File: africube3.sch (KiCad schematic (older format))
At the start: 36 parts, among them IC1 ADC-20-4, J1 SMA Edge FM, J2 Conn_01x04, J3 RPi_GPIO, J4 Conn_01x02, U1 TQP7M9105, U2 SXBP-150+, U3 BA178M05FP-E2, U4 MCP3421A0T-E/CH

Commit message: removing power detector
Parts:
- removed C8: 100pF, Capacitors_SMD:C_0805_HandSoldering, symbol C_Small
- removed C?: 1nF, Capacitors_SMD:C_0805_HandSoldering, symbol C_Small
- removed D2: SMS3922-079LF, symbol D_Schottky
- removed IC1: ADC-20-4, ADC-20-4+, symbol ADC-20-4
- removed R3: 50, Resistors_SMD:R_0805_HandSoldering, symbol R
- removed R6, R7, R8, R9: 220K, Resistors_SMD:R_0805_HandSoldering, symbol R
- removed U4: MCP3421A0T-E/CH, symbol MCP3421A0T-E/CH
- U3: footprint TO_SOT_Packages_SMD:TO-252-3_TabPin2 -> TO_SOT_Packages_SMD:TO-252-3_TabPin4
- renumbered C11 to C10, C9 to C8, C10 to C9, R4 to R3, R5 to R4
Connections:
- net at J1.1 (In): now also U2.8 (RF_OUT)
- net SCL: no longer names the net of J3.5 (GPIO03_SCL1_I2C)
- net SDA: no longer names the net of J3.3 (GPIO02_SDA1_I2C)
- no-connect marks 25 -> 27
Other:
- moved on the sheet: J1

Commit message: removed power detection
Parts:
- U2: footprint RF_Mini-Circuits:Mini-Circuits_HF1139_LandPatternPL-230 -> mini_filter:Mini-Circuits_HF1139_LandPatternPL-230
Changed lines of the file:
@@
 LIBS:ADC-15-4+
 LIBS:AD8317
+LIBS:africube3-cache
 EELAYER 25 0
 EELAYER END
@@
 F 0 "U2" H 7200 1800 60  0000 C CNN
 F 1 "SXBP-150+" H 7200 2300 60  0000 C CNN
-F 2 "RF_Mini-Circuits:Mini-Circuits_HF1139_LandPatternPL-230" H 7200 1900 60  0001 C CNN
+F 2 "mini_filter:Mini-Circuits_HF1139_LandPatternPL-230" H 7200 1900 60  0001 C CNN
 F 3 "" H 7200 1900 60  0001 C CNN
 	1    7200 2050

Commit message: layout done need to do groundplanes
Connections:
- net GND: now also J2.4 (Pin_4), U3.2 (GND)
- now unconnected: J3.1 (3.3V), J3.17 (3.3V)
- no-connect marks 27 -> 29
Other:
- moved on the sheet: C9
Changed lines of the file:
@@
 L GND #PWR016
 U 1 1 5D290BB7
-P 5650 3350
-F 0 "#PWR016" H 5650 3100 50  0001 C CNN
-F 1 "GND" H 5650 3200 50  0000 C CNN
-F 2 "" H 5650 3350 50  0001 C CNN
-F 3 "" H 5650 3350 50  0001 C CNN
-	1    5650 3350
+P 5550 3350
+F 0 "#PWR016" H 5550 3100 50  0001 C CNN
+F 1 "GND" H 5550 3200 50  0000 C CNN
+F 2 "" H 5550 3350 50  0001 C CNN
+F 3 "" H 5550 3350 50  0001 C CNN
+	1    5550 3350
 	1    0    0    -1
 $EndComp
@@
 L CP_Small C9
 U 1 1 5D290DB1
-P 5650 3150
-F 0 "C9" H 5500 3050 50  0000 L CNN
-F 1 "4.7uF 16V" H 5400 3450 50  0000 L CNN
-F 2 "Capacitors_SMD:C_0805_HandSoldering" H 5650 3150 50  0001 C CNN
-F 3 "" H 5650 3150 50  0001 C CNN
-	1    5650 3150
+P 5550 3150
+F 0 "C9" H 5400 3050 50  0000 L CNN
+F 1 "4.7uF 16V" H 5300 3450 50  0000 L CNN
+F 2 "Capacitors_SMD:C_0805_HandSoldering" H 5550 3150 50  0001 C CNN
+F 3 "" H 5550 3150 50  0001 C CNN
+	1    5550 3150
 	1    0    0    -1
 $EndComp
@@
 	5150 3100 5250 3100
 Wire Wire Line
-	5650 3050 5650 3000
-Connection ~ 5650 3000
-Wire Wire Line
-	5650 3250 5650 3350
-Wire Wire Line
 	6650 3000 7150 3000
-Wire Wire Line
-	5350 2800 5350 3450
-Wire Wire Line
-	5350 3450 2850 3450
-Wire Wire Line
-	2850 3450 2850 3750
-Wire Wire Line
-	2700 3750 3000 3750
-Wire Wire Line
-	3000 4550 2700 4550
-Wire Wire Line
-	2700 4550 2700 3750
-Connection ~ 2850 3750
 Wire Wire Line
 	2800 4950 3000 4950
@@
 	2950 1950 2950 1900
 Connection ~ 2950 1900
-Wire Wire Line
-	5350 2800 5150 2800
 Wire Wire Line
 	5300 2700 5300 2900
@@
 NoConn ~ 3000 3850
 NoConn ~ 3000 3950
+NoConn ~ 3000 3750
+NoConn ~ 3000 4550
+$Comp
+L GND #PWR025
+U 1 1 5D701E2B
+P 5200 2400
+F 0 "#PWR025" H 5200 2150 50  0001 C CNN
+F 1 "GND" H 5200 2250 50  0000 C CNN
+F 2 "" H 5200 2400 50  0001 C CNN
+F 3 "" H 5200 2400 50  0001 C CNN
+	1    5200 2400
+	-1   0    0    1
+$EndComp
+Wire Wire Line
+	5200 2400 5200 2800
+Wire Wire Line
+	5200 2800 5150 2800
+Wire Wire Line
+	5550 3000 5550 3050
+Connection ~ 5550 3000
+Wire Wire Line
+	5550 3250 5550 3350
+$Comp
+L GND #PWR?
+U 1 1 5D7024AE
+P 5750 3300
+F 0 "#PWR?" H 5750 3050 50  0001 C CNN
+F 1 "GND" H 5750 3150 50  0000 C CNN
+F 2 "" H 5750 3300 50  0001 C CNN
+F 3 "" H 5750 3300 50  0001 C CNN
+	1    5750 3300
+	1    0    0    -1
+$EndComp
+Wire Wire Line
+	5750 3150 5750 3300
 $EndSCHEMATC

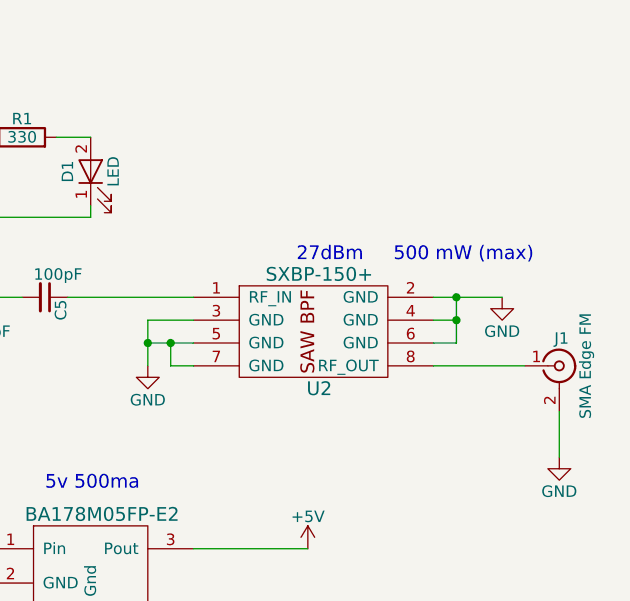
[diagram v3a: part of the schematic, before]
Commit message: added groundplane
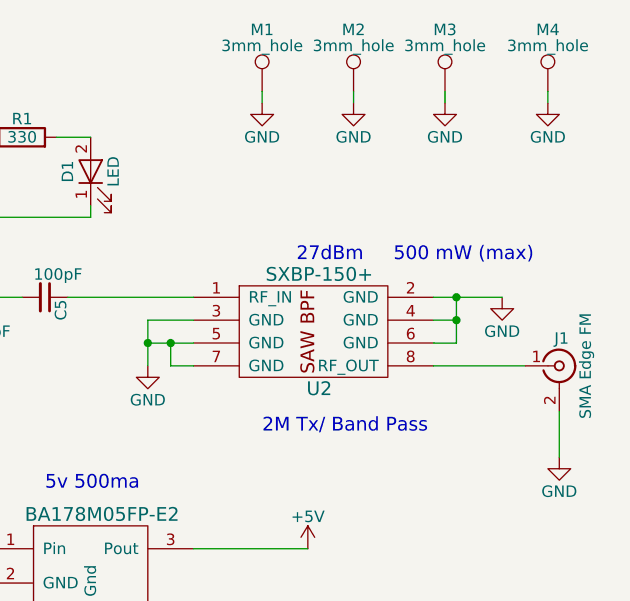
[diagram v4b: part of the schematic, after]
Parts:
- added M1, M2, M3, M4: 3mm_hole, 3mm_Mounting_Hole, symbol TEST_1P
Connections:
- net GND: now also M1.1, M2.1, M3.1, M4.1
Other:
- note added: "2M Tx/ Band Pass"
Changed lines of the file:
@@
 	5550 3250 5550 3350
 $Comp
-L GND #PWR?
+L GND #PWR026
 U 1 1 5D7024AE
 P 5750 3300
-F 0 "#PWR?" H 5750 3050 50  0001 C CNN
+F 0 "#PWR026" H 5750 3050 50  0001 C CNN
 F 1 "GND" H 5750 3150 50  0000 C CNN
 F 2 "" H 5750 3300 50  0001 C CNN
@@
 Wire Wire Line
 	5750 3150 5750 3300
+$Comp
+L TEST_1P M1
+U 1 1 5D715A60
+P 6950 1000
+F 0 "M1" H 6950 1270 50  0000 C CNN
+F 1 "3mm_hole" H 6950 1200 50  0000 C CNN
+F 2 "3mm_Mounting_Hole" H 7150 1000 50  0001 C CNN
+F 3 "" H 7150 1000 50  0001 C CNN
+	1    6950 1000
+	1    0    0    -1
+$EndComp
+$Comp
+L TEST_1P M2
+U 1 1 5D715AD8
+P 7350 1000
+F 0 "M2" H 7350 1270 50  0000 C CNN
+F 1 "3mm_hole" H 7350 1200 50  0000 C CNN
+F 2 "3mm_Mounting_Hole" H 7550 1000 50  0001 C CNN
+F 3 "" H 7550 1000 50  0001 C CNN
+	1    7350 1000
+	1    0    0    -1
+$EndComp
+$Comp
+L TEST_1P M3
+U 1 1 5D715B54
+P 7750 1000
+F 0 "M3" H 7750 1270 50  0000 C CNN
+F 1 "3mm_hole" H 7750 1200 50  0000 C CNN
+F 2 "3mm_Mounting_Hole" H 7950 1000 50  0001 C CNN
+F 3 "" H 7950 1000 50  0001 C CNN
+	1    7750 1000
+	1    0    0    -1
+$EndComp
+$Comp
+L TEST_1P M4
+U 1 1 5D715BCD
+P 8200 1000
+F 0 "M4" H 8200 1270 50  0000 C CNN
+F 1 "3mm_hole" H 8200 1200 50  0000 C CNN
+F 2 "3mm_Mounting_Hole" H 8400 1000 50  0001 C CNN
+F 3 "" H 8400 1000 50  0001 C CNN
+	1    8200 1000
+	1    0    0    -1
+$EndComp
+$Comp
+L GND #PWR027
+U 1 1 5D715C43
+P 6950 1050
+F 0 "#PWR027" H 6950 800 50  0001 C CNN
+F 1 "GND" H 6950 900 50  0000 C CNN
+F 2 "" H 6950 1050 50  0001 C CNN
+F 3 "" H 6950 1050 50  0001 C CNN
+	1    6950 1050
+	1    0    0    -1
+$EndComp
+$Comp
+L GND #PWR028
+U 1 1 5D715CA8
+P 7350 1050
+F 0 "#PWR028" H 7350 800 50  0001 C CNN
+F 1 "GND" H 7350 900 50  0000 C CNN
+F 2 "" H 7350 1050 50  0001 C CNN
+F 3 "" H 7350 1050 50  0001 C CNN
+	1    7350 1050
+	1    0    0    -1
+$EndComp
+$Comp
+L GND #PWR029
+U 1 1 5D715D0D
+P 7750 1050
+F 0 "#PWR029" H 7750 800 50  0001 C CNN
+F 1 "GND" H 7750 900 50  0000 C CNN
+F 2 "" H 7750 1050 50  0001 C CNN
+F 3 "" H 7750 1050 50  0001 C CNN
+	1    7750 1050
+	1    0    0    -1
+$EndComp
+$Comp
+L GND #PWR030
+U 1 1 5D715D72
+P 8200 1050
+F 0 "#PWR030" H 8200 800 50  0001 C CNN
+F 1 "GND" H 8200 900 50  0000 C CNN
+F 2 "" H 8200 1050 50  0001 C CNN
+F 3 "" H 8200 1050 50  0001 C CNN
+	1    8200 1050
+	1    0    0    -1
+$EndComp
+Wire Wire Line
+	6950 1000 6950 1050
+Wire Wire Line
+	7350 1000 7350 1050
+Wire Wire Line
+	7750 1000 7750 1050
+Wire Wire Line
+	8200 1000 8200 1050
+Text Notes 6950 2500 0    60   ~ 0
+2M Tx/ Band Pass
 $EndSCHEMATC
